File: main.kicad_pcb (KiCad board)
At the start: 2 copper layers, 65 x 56 mm, 70 parts, among them J2 mini iso blue, J3 LCD power, J7 Programming Socket, P1 Conn_02x20_Odd_Even, Q1 NPN, Q2 NPN, SW1 EN, SW2 EN, U1 TJA1051TK-3, U10 NTS0104GU12_115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

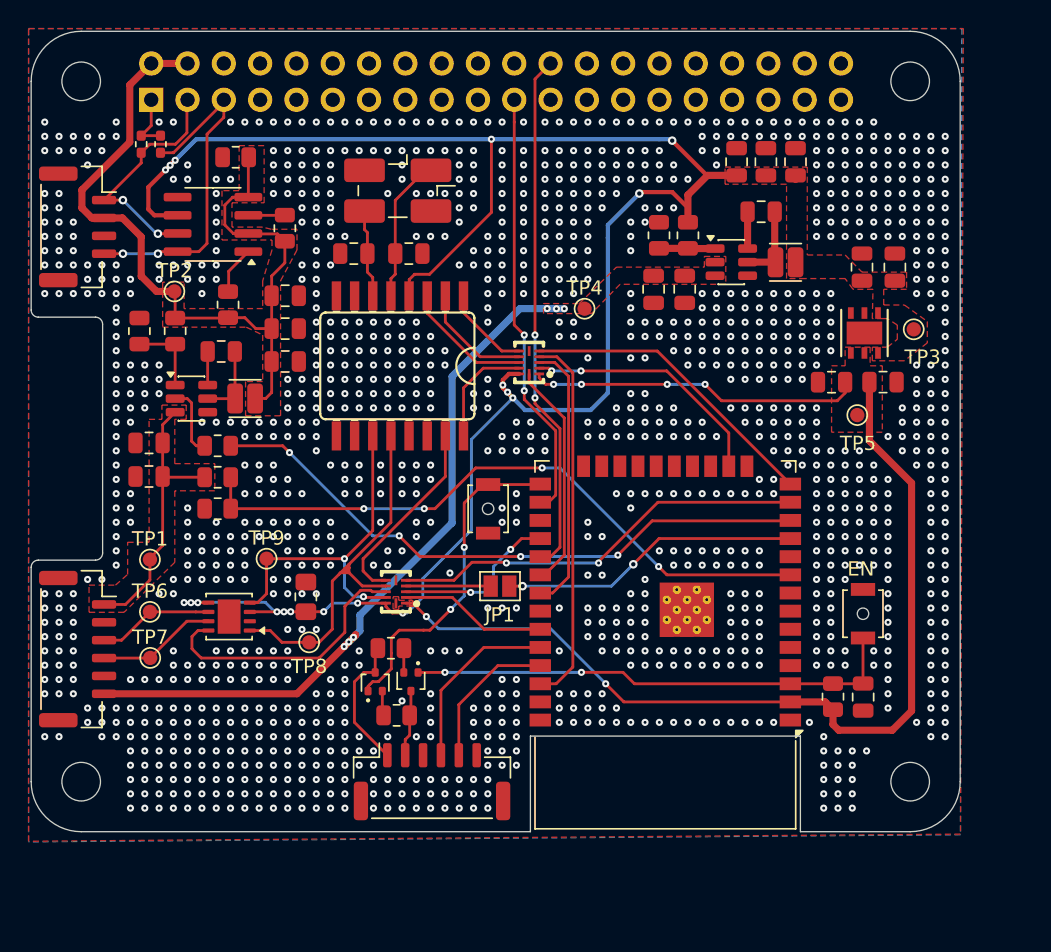
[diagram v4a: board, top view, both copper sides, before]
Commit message: added 3D models; light touch-ups
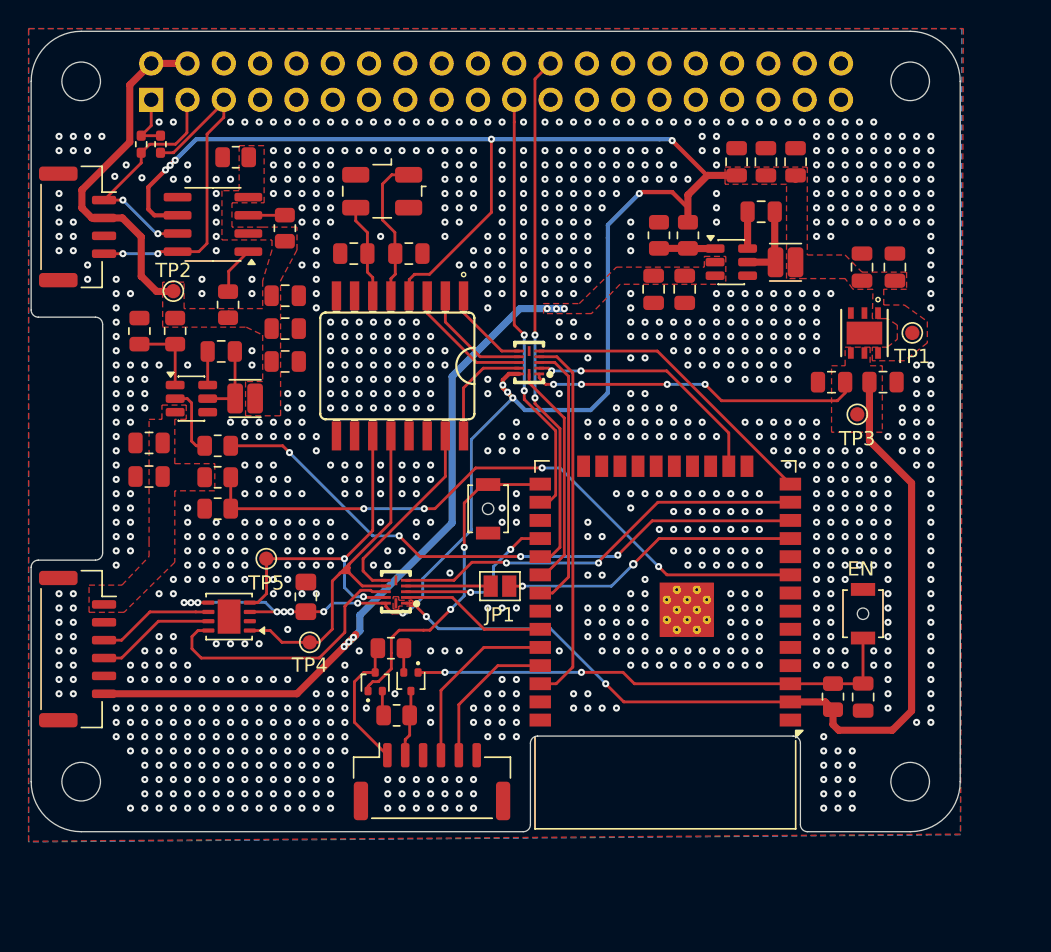
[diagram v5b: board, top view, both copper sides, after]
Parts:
- removed TP6, TP7, TP8, TP9: TestPoint, TestPoint:TestPoint_Pad_D1.0mm
- U8: footprint Crystal:Crystal_SMD_EuroQuartz_MJ-4Pin_5.0x3.2mm_HandSoldering -> Crystal:Crystal_SMD_EuroQuartz_MJ-4Pin_5.0x3.2mm
- moved TP1 55.6 mm to (165.3, 102.3)
- moved TP5 42.6 mm to (120.1, 118.1)
- moved TP4 30.2 mm to (123.2, 123.9)
- moved TP3 7.14 mm to (161.5, 108.0)
- moved U8 1.09 mm to (128.2, 92.4)
- moved TP2 0.07 mm to (113.6, 99.4)
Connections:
- TP1 pad 1: +12V Ignition -> +5V Car Battery
- TP3 pad 1: +5V Car Battery -> +3V3 Car Battery
- TP4 pad 1: +12V Car Battery -> VAN_TX
- TP5 pad 1: +3V3 Car Battery -> VAN_RX
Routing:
- net +5V Ignition: track 57.2 -> 25.4 mm
- net +12V Ignition: track 19.3 -> 0.20 mm
- net GND: vias 1308 -> 1122
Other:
- outline, holes or cut-outs redrawn

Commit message: switched to vertial program connector, changed logo position
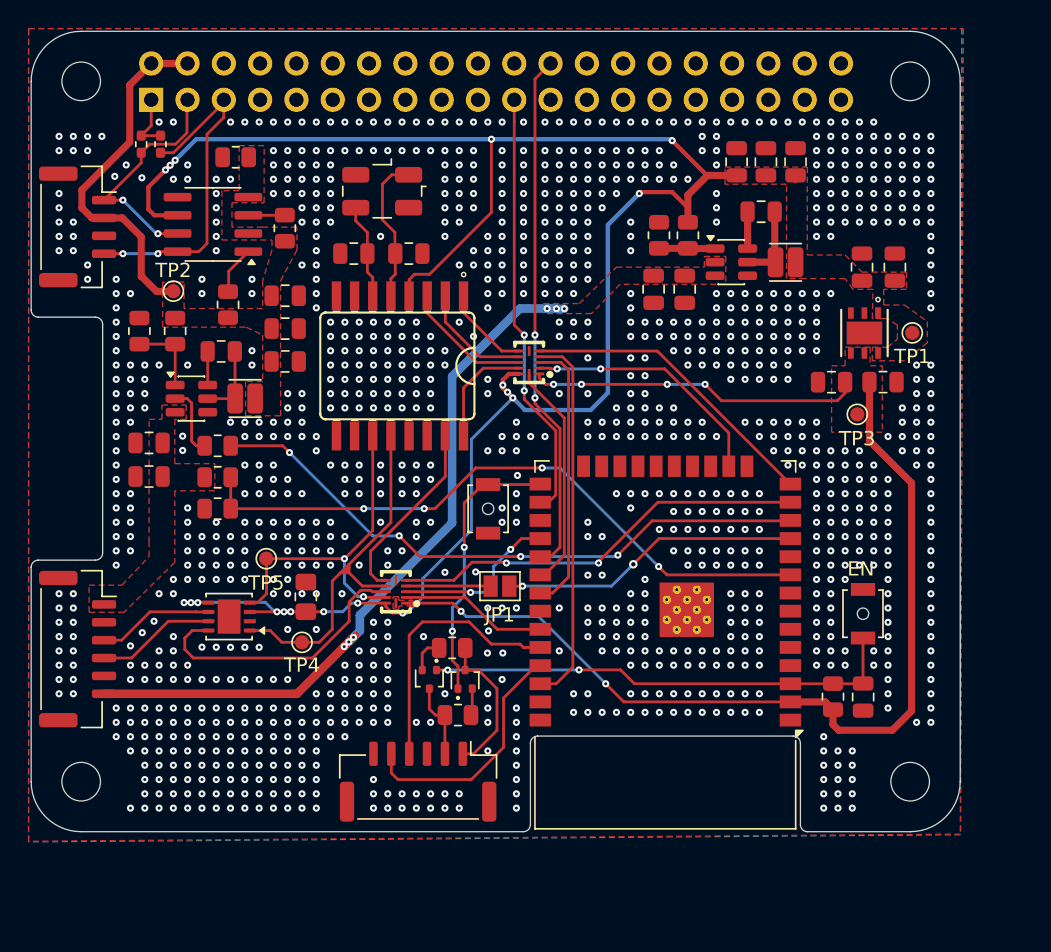
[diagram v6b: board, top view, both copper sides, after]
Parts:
- J7: footprint Connector_JST:JST_GH_SM06B-GHS-TB_1x06-1MP_P1.25mm_Horizontal -> Connector_JST:JST_GH_BM06B-GHS-TBT_1x06-1MP_P1.25mm_Vertical
- moved G*** 18.2 mm to (151.8, 106.5), turned to -90 degrees
- moved Q2 6.29 mm to (134.0, 126.5)
- moved R20 4.29 mm to (133.1, 124.3), turned to 180 degrees
- moved R22 4.29 mm to (133.5, 129.0), turned to 0 degrees
- moved Q1 1.30 mm to (131.5, 126.5)
- moved J7 0.97 mm to (130.8, 133.7), turned to 180 degrees
- moved TP4 0.54 mm to (122.6, 123.9)
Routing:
- net TX: track 10.4 -> 17.3 mm
- net RX: track 12.7 -> 18.6 mm
- net GPIO0: track 23.3 -> 19.4 mm
- net EN: track 34.7 -> 33.5 mm
- net RTS: track 4.66 -> 5.73 mm
- net Net-(Q1-B): track 1.71 -> 2.52 mm
- net DTR: track 9.59 -> 10.3 mm
- net TJA_S: track 19.1 -> 19.8 mm
- net TSS_CLK: track 13.7 -> 13.1 mm
- net GND: vias 1122 -> 1162

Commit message: added tvs diodes, 100nF, pull-up for TSS interrupt
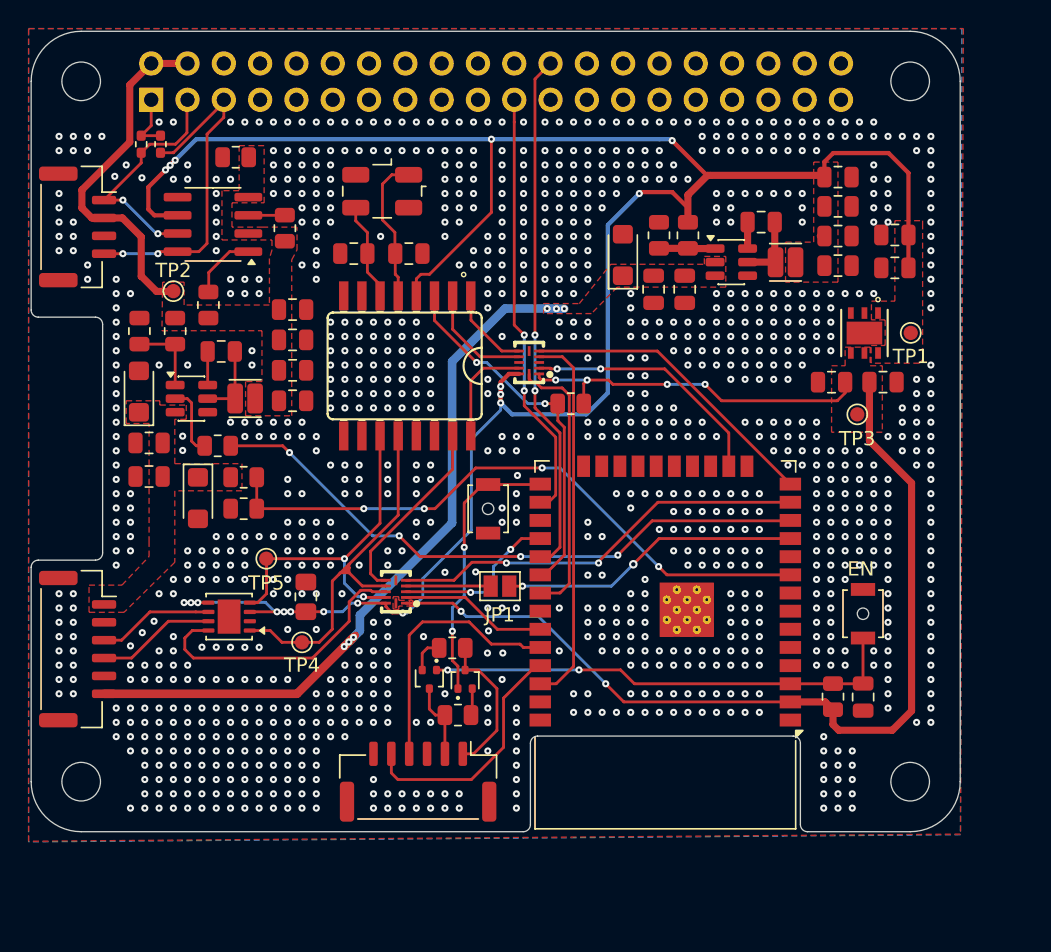
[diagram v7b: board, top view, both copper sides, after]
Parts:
- added C22: 100nF, Capacitor_SMD:C_0805_2012Metric, F.Cu at (122.0, 100.7)
- added C23: 100nF, Capacitor_SMD:C_0805_2012Metric, F.Cu at (160.1, 97.6)
- added R9: 4k7, Resistor_SMD:R_0805_2012Metric, F.Cu at (141.4, 107.2)
- added U12: VTVS25ASMF-HM3-08, Diode_SMD:D_SMF, F.Cu at (111.2, 106.4)
- added U13: VTVS25ASMF-HM3-08, Diode_SMD:D_SMF, F.Cu at (115.3, 113.8)
- added U9: VTVS25ASMF-HM3-08, Diode_SMD:D_SMF, F.Cu at (145.1, 96.8)
- moved C6 7.18 mm to (160.1, 91.4), turned to 0 degrees
- moved C15 5.98 mm to (160.1, 95.5), turned to 0 degrees
- moved C14 5.93 mm to (160.1, 93.4), turned to 0 degrees
- moved C21 3.13 mm to (122.0, 102.8)
- moved C20 2.97 mm to (122.0, 104.9)
- moved C19 2.80 mm to (122.0, 107.0)
- moved C13 2.30 mm to (164.1, 97.7), turned to 180 degrees
- moved C11 2.25 mm to (164.1, 95.4), turned to 0 degrees
- moved R2 1.82 mm to (118.5, 112.4)
- moved R3 1.82 mm to (118.5, 114.6)
- moved R6 1.38 mm to (116.1, 100.3)
- moved C5 0.73 mm to (154.8, 94.5)
- moved U3 0.51 mm to (129.4, 104.6)
- moved TP1 0.11 mm to (165.2, 102.3)
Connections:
- U10 pad 3: TSS Interrupt 3.3V -> unconnected-(U10-A2-Pad3)
- U10 pad 9: TSS Interrupt 5V -> unconnected-(U10-B2-Pad9)
- U3 pad 3: TSS Interrupt 5V -> TSS Interrupt
- U6 pad 30: ESP_TSS_OE -> TSS Interrupt
- U6 pad 31: TSS Interrupt 3.3V -> ESP_TSS_OE
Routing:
- net TSS Interrupt: track 0.00 -> 25.8 mm, vias 0 -> 2
- net TSS Interrupt 3.3V: track 19.2 -> 0.00 mm
- net +5V Car Battery: track 139.4 -> 158.1 mm
- net TSS Interrupt 5V: track 9.08 -> 0.00 mm
- net ESP_TSS_OE: track 16.0 -> 19.1 mm
- net ESP_ADC1_CH5: track 45.7 -> 43.8 mm
- net +3V3 Car Battery: track 87.8 -> 89.5 mm
- net Net-(U7-32KHZ): track 2.95 -> 4.66 mm
- net Net-(U4-SW): track 5.44 -> 4.72 mm
- net Net-(U4-BST): track 2.58 -> 1.85 mm
- net +12V Car Battery: track 50.8 -> 51.4 mm
- net GND: vias 1162 -> 1108

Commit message: Modified ADC resistors. Added bypass cap to ADC.
Removed some ground islands.
Removed lock files and added them to gitignore.
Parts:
- added C24: 100nF, Capacitor_SMD:C_0805_2012Metric, F.Cu at (159.2, 117.0)
- R2: value 2M -> 90k
- R3: value 523k -> 10k
- renumbered TP3 to 3V3_B1, TP1 to 5V_B1, TP2 to 5V_I1, TP5 to V_RX1, TP4 to V_TX1
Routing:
- net ESP_ADC1_CH5: track 43.8 -> 49.4 mm
- net SDA: track 16.6 -> 16.1 mm
- net GND: vias 1108 -> 946
